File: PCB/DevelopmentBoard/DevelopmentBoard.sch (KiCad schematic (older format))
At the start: 11 parts

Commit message: Schematic Capture for RF module
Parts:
- added R? (x2): 4.7k, symbol Device:R_Small_US
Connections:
- net labels added: TBS_Crossfire_SCL, TBS_Crossfire_SDA
- wire segments 12 -> 19
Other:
- moved on the sheet: R?
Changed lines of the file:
@@
 L Device:R_Small_US R?
 U 1 1 6166A727
-P 6150 6050
-F 0 "R?" H 6218 6096 50  0000 L CNN
-F 1 "4.7k" H 6218 6005 50  0000 L CNN
-F 2 "" H 6150 6050 50  0001 C CNN
-F 3 "~" H 6150 6050 50  0001 C CNN
-	1    6150 6050
+P 6250 6050
+F 0 "R?" H 6318 6096 50  0000 L CNN
+F 1 "4.7k" H 6318 6005 50  0000 L CNN
+F 2 "" H 6250 6050 50  0001 C CNN
+F 3 "~" H 6250 6050 50  0001 C CNN
+	1    6250 6050
 	1    0    0    -1
 $EndComp
@@
 L Device:R_Small_US R?
 U 1 1 6166AB22
-P 6450 6050
-F 0 "R?" H 6518 6096 50  0000 L CNN
-F 1 "4.7k" H 6518 6005 50  0000 L CNN
-F 2 "" H 6450 6050 50  0001 C CNN
-F 3 "~" H 6450 6050 50  0001 C CNN
-	1    6450 6050
+P 6550 6050
+F 0 "R?" H 6618 6096 50  0000 L CNN
+F 1 "4.7k" H 6618 6005 50  0000 L CNN
+F 2 "" H 6550 6050 50  0001 C CNN
+F 3 "~" H 6550 6050 50  0001 C CNN
+	1    6550 6050
 	1    0    0    -1
 $EndComp
@@
 	5850 6150 5850 6750
 Wire Wire Line
-	6450 6150 6450 6750
-Text Label 6450 6150 3    50   ~ 0
+	6550 6150 6550 6750
+Text Label 6550 6150 3    50   ~ 0
 VN-100_MOSI
 Wire Wire Line
-	6150 6750 6150 6150
-Text Label 6150 6150 3    50   ~ 0
+	6250 6750 6250 6150
+Text Label 6250 6150 3    50   ~ 0
 VN-100_MISO
 $Comp
@@
 L power:+3.3V #PWR?
 U 1 1 61671A73
-P 6150 5950
-F 0 "#PWR?" H 6150 5800 50  0001 C CNN
-F 1 "+3.3V" H 6165 6123 50  0000 C CNN
-F 2 "" H 6150 5950 50  0001 C CNN
-F 3 "" H 6150 5950 50  0001 C CNN
-	1    6150 5950
+P 6250 5950
+F 0 "#PWR?" H 6250 5800 50  0001 C CNN
+F 1 "+3.3V" H 6265 6123 50  0000 C CNN
+F 2 "" H 6250 5950 50  0001 C CNN
+F 3 "" H 6250 5950 50  0001 C CNN
+	1    6250 5950
 	1    0    0    -1
 $EndComp
@@
 L power:+3.3V #PWR?
 U 1 1 61672A6F
-P 6450 5950
-F 0 "#PWR?" H 6450 5800 50  0001 C CNN
-F 1 "+3.3V" H 6465 6123 50  0000 C CNN
-F 2 "" H 6450 5950 50  0001 C CNN
-F 3 "" H 6450 5950 50  0001 C CNN
-	1    6450 5950
+P 6550 5950
+F 0 "#PWR?" H 6550 5800 50  0001 C CNN
+F 1 "+3.3V" H 6565 6123 50  0000 C CNN
+F 2 "" H 6550 5950 50  0001 C CNN
+F 3 "" H 6550 5950 50  0001 C CNN
+	1    6550 5950
 	1    0    0    -1
 $EndComp
+Wire Wire Line
+	17700 7600 17500 7600
+Connection ~ 17500 7600
+Text Label 16850 7700 0    50   ~ 0
+TBS_Crossfire_SCL
+Text Label 16850 7600 0    50   ~ 0
+TBS_Crossfire_SDA
+Wire Wire Line
+	16850 7600 17500 7600
+Wire Wire Line
+	16850 7700 17500 7700
+Text Label 10550 8150 0    50   ~ 0
+TBS_Crossfire_SCL
+Text Label 10550 8250 0    50   ~ 0
+TBS_Crossfire_SDA
+Wire Wire Line
+	10550 8250 11250 8250
+Wire Wire Line
+	10550 8150 11250 8150
+$Comp
+L Device:R_Small_US R?
+U 1 1 6160D96F
+P 5850 7300
+F 0 "R?" H 5918 7346 50  0000 L CNN
+F 1 "4.7k" H 5918 7255 50  0000 L CNN
+F 2 "" H 5850 7300 50  0001 C CNN
+F 3 "~" H 5850 7300 50  0001 C CNN
+	1    5850 7300
+	1    0    0    -1
+$EndComp
+$Comp
+L Device:R_Small_US R?
+U 1 1 6160D975
+P 6150 7300
+F 0 "R?" H 6218 7346 50  0000 L CNN
+F 1 "4.7k" H 6218 7255 50  0000 L CNN
+F 2 "" H 6150 7300 50  0001 C CNN
+F 3 "~" H 6150 7300 50  0001 C CNN
+	1    6150 7300
+	1    0    0    -1
+$EndComp
+Text Label 6150 7400 3    50   ~ 0
+TBS_Crossfire_SCL
+Text Label 5850 7400 3    50   ~ 0
+TBS_Crossfire_SDA
+$Comp
+L power:+3.3V #PWR?
+U 1 1 6160D97F
+P 5850 7200
+F 0 "#PWR?" H 5850 7050 50  0001 C CNN
+F 1 "+3.3V" H 5865 7373 50  0000 C CNN
+F 2 "" H 5850 7200 50  0001 C CNN
+F 3 "" H 5850 7200 50  0001 C CNN
+	1    5850 7200
+	1    0    0    -1
+$EndComp
+$Comp
+L power:+3.3V #PWR?
+U 1 1 6160D985
+P 6150 7200
+F 0 "#PWR?" H 6150 7050 50  0001 C CNN
+F 1 "+3.3V" H 6165 7373 50  0000 C CNN
+F 2 "" H 6150 7200 50  0001 C CNN
+F 3 "" H 6150 7200 50  0001 C CNN
+	1    6150 7200
+	1    0    0    -1
+$EndComp
+Wire Wire Line
+	6150 7400 6150 8100
+Wire Wire Line
+	5850 7400 5850 8100
+$Comp
+L power:GND #PWR?
+U 1 1 61619131
+P 18300 7400
+F 0 "#PWR?" H 18300 7150 50  0001 C CNN
+F 1 "GND" V 18305 7272 50  0000 R CNN
+F 2 "" H 18300 7400 50  0001 C CNN
+F 3 "" H 18300 7400 50  0001 C CNN
+	1    18300 7400
+	0    -1   -1   0
+$EndComp
+$Comp
+L power:GND #PWR?
+U 1 1 6161AEF3
+P 17500 7500
+F 0 "#PWR?" H 17500 7250 50  0001 C CNN
+F 1 "GND" V 17505 7372 50  0000 R CNN
+F 2 "" H 17500 7500 50  0001 C CNN
+F 3 "" H 17500 7500 50  0001 C CNN
+	1    17500 7500
+	0    1    1    0
+$EndComp
+$Comp
+L power:+5V #PWR?
+U 1 1 6161BA5A
+P 18300 7500
+F 0 "#PWR?" H 18300 7350 50  0001 C CNN
+F 1 "+5V" V 18315 7628 50  0000 L CNN
+F 2 "" H 18300 7500 50  0001 C CNN
+F 3 "" H 18300 7500 50  0001 C CNN
+	1    18300 7500
+	0    1    1    0
+$EndComp
 $EndSCHEMATC

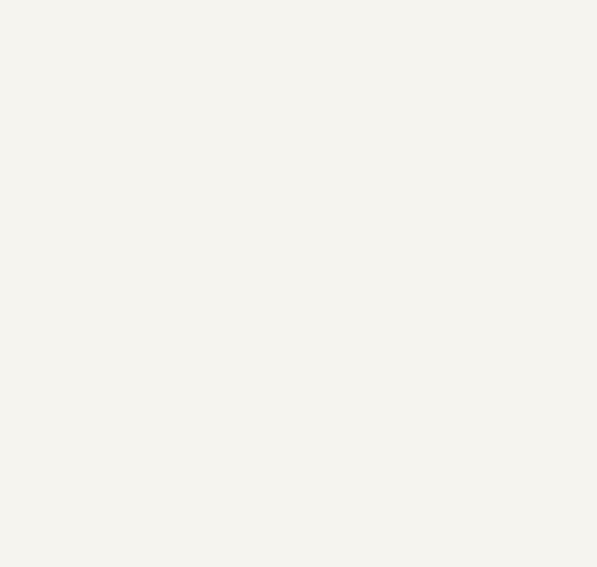
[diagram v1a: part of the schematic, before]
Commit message: Placed Micro-USB symbol on schematic
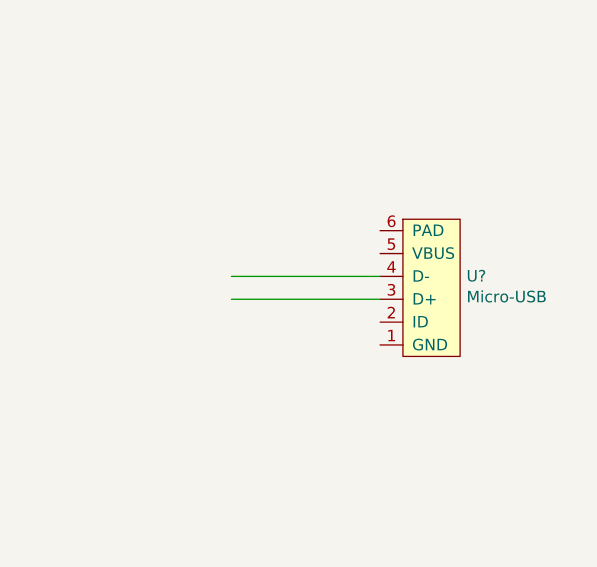
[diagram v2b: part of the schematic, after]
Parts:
- added U?: Micro-USB, symbol PayloadSymbols:Micro-USB
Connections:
- wire segments 19 -> 21
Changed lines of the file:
@@
 	0    1    1    0
 $EndComp
+$Comp
+L PayloadSymbols:Micro-USB U?
+U 1 1 615E85F0
+P 20550 7750
+F 0 "U?" H 20728 7801 50  0000 L CNN
+F 1 "Micro-USB" H 20728 7710 50  0000 L CNN
+F 2 "" H 20450 7800 50  0001 C CNN
+F 3 "" H 20450 7800 50  0001 C CNN
+	1    20550 7750
+	1    0    0    -1
+$EndComp
+Wire Wire Line
+	19700 7700 20350 7700
+Wire Wire Line
+	19700 7800 20350 7800
 $EndSCHEMATC

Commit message: USB Pins
Found and connected the USB pins on pins 103 & 105
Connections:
- net labels added: USB_D+, USB_D-
- wire segments 21 -> 23
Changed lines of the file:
@@
 Wire Wire Line
 	19700 7800 20350 7800
+Wire Wire Line
+	13400 4350 13050 4350
+Wire Wire Line
+	13400 4450 13050 4450
+Text Label 13400 4350 2    50   ~ 0
+USB_D-
+Text Label 13400 4450 2    50   ~ 0
+USB_D+
+Text Label 20200 7700 2    50   ~ 0
+USB_D-
+Text Label 20200 7800 2    50   ~ 0
+USB_D+
 $EndSCHEMATC

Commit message: Finished VN-100 Breakout Board. Removed USB from DevBoard Schematic
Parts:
- removed U?: Micro-USB, symbol PayloadSymbols:Micro-USB
- removed X?: XT30-F_Connector, symbol PayloadSymbols:XT30-F_Connector
- added X?: XT30-F_Connector, symbol PayloadSymbols:XT30-F_Connector
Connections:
- net labels removed: USB_D+, USB_D-
- wire segments 23 -> 21
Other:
- moved on the sheet: U?, X?

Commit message: Updated Dev Board Schematic
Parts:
- removed U?: VN-100, symbol PayloadSymbols:VN-100
- added R? (x12): 0, symbol Device:R_Small_US
- added U?: Micro-USB, symbol PayloadSymbols:Micro-USB
- added U?: Barometer_Grove, symbol PayloadSymbols:Barometer_Grove
- added U?: VN-100_Breakout, symbol PayloadSymbols:VN-100_Breakout
- added X?: 2mmGrove_Connector, symbol PayloadSymbols:2mmGrove_Connector
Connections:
- net labels added: D+, D-, MCU_Reset, RX, SCL, SDA, TX, VN-100_Enable
- net labels removed: TBS_Crossfire_SCL, TBS_Crossfire_SDA
- wire segments 21 -> 35
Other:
- note added: "High during ON: Reset\n"
- note added: "Low: Disable\n"
- note added: "Low: Reset"
- moved on the sheet: R?

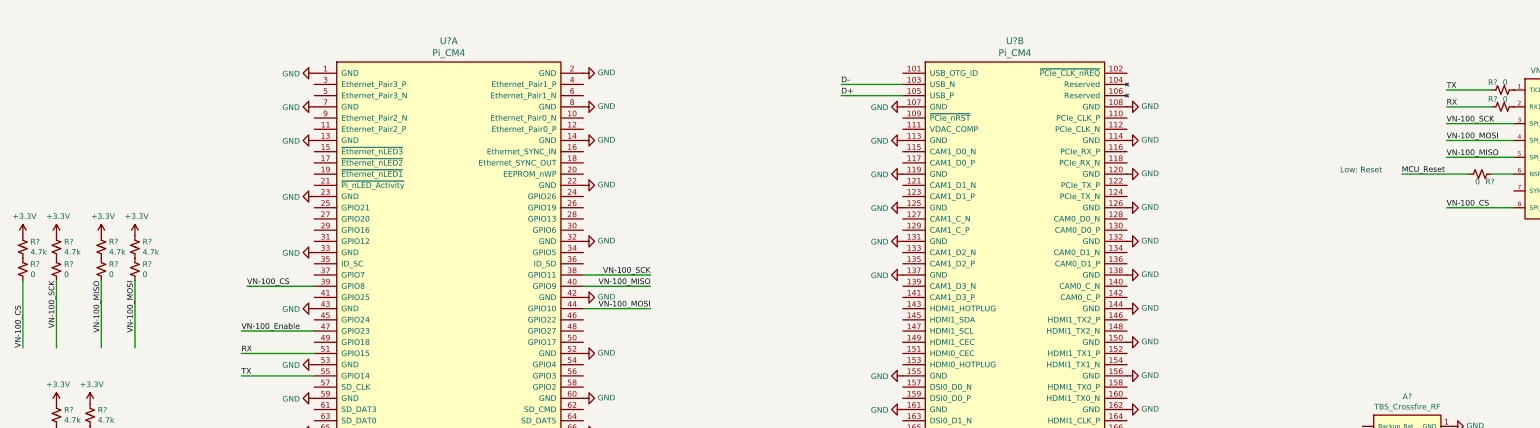
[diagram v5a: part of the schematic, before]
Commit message: Devboard changes(UART & SPI)
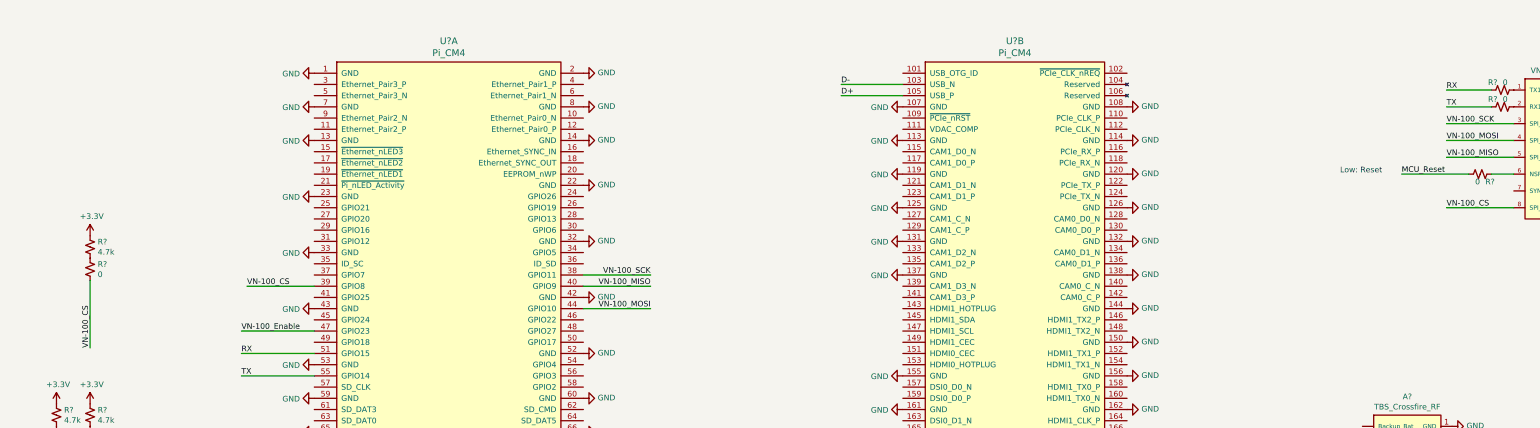
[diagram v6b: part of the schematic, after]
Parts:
- removed R? (x3): 4.7k, symbol Device:R_Small_US
- removed R? (x3): 0, symbol Device:R_Small_US
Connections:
- wire segments 35 -> 32
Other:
- moved on the sheet: R?
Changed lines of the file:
@@
-$Comp
-L Device:R_Small_US R?
-U 1 1 616692E6
-P 5850 5800
-F 0 "R?" H 5918 5846 50  0000 L CNN
-F 1 "4.7k" H 5918 5755 50  0000 L CNN
-F 2 "" H 5850 5800 50  0001 C CNN
-F 3 "~" H 5850 5800 50  0001 C CNN
-	1    5850 5800
-	1    0    0    -1
-$EndComp
-$Comp
-L Device:R_Small_US R?
-U 1 1 6166A727
-P 6250 5800
-F 0 "R?" H 6318 5846 50  0000 L CNN
-F 1 "4.7k" H 6318 5755 50  0000 L CNN
-F 2 "" H 6250 5800 50  0001 C CNN
-F 3 "~" H 6250 5800 50  0001 C CNN
-	1    6250 5800
-	1    0    0    -1
-$EndComp
-$Comp
-L Device:R_Small_US R?
-U 1 1 6166AB22
-P 6550 5800
-F 0 "R?" H 6618 5846 50  0000 L CNN
-F 1 "4.7k" H 6618 5755 50  0000 L CNN
-F 2 "" H 6550 5800 50  0001 C CNN
-F 3 "~" H 6550 5800 50  0001 C CNN
-	1    6550 5800
-	1    0    0    -1
-$EndComp
 $Comp
 L Device:R_Small_US R?
 U 1 1 6166E291
-P 5550 5800
-F 0 "R?" H 5618 5846 50  0000 L CNN
-F 1 "4.7k" H 5618 5755 50  0000 L CNN
-F 2 "" H 5550 5800 50  0001 C CNN
-F 3 "~" H 5550 5800 50  0001 C CNN
-	1    5550 5800
-	1    0    0    -1
-$EndComp
-Wire Wire Line
-	5550 6100 5550 6700
-Text Label 5550 6700 1    50   ~ 0
+P 6150 5800
+F 0 "R?" H 6218 5846 50  0000 L CNN
+F 1 "4.7k" H 6218 5755 50  0000 L CNN
+F 2 "" H 6150 5800 50  0001 C CNN
+F 3 "~" H 6150 5800 50  0001 C CNN
+	1    6150 5800
+	1    0    0    -1
+$EndComp
+Wire Wire Line
+	6150 6100 6150 6700
+Text Label 6150 6700 1    50   ~ 0
 VN-100_CS
-Text Label 5850 6100 3    50   ~ 0
-VN-100_SCK
-Wire Wire Line
-	5850 6100 5850 6700
-Wire Wire Line
-	6550 6100 6550 6700
-Text Label 6550 6100 3    50   ~ 0
-VN-100_MOSI
-Wire Wire Line
-	6250 6700 6250 6100
-Text Label 6250 6100 3    50   ~ 0
-VN-100_MISO
 $Comp
 L power:+3.3V #PWR?
 U 1 1 61670634
-P 5550 5700
-F 0 "#PWR?" H 5550 5550 50  0001 C CNN
-F 1 "+3.3V" H 5565 5873 50  0000 C CNN
-F 2 "" H 5550 5700 50  0001 C CNN
-F 3 "" H 5550 5700 50  0001 C CNN
-	1    5550 5700
-	1    0    0    -1
-$EndComp
-$Comp
-L power:+3.3V #PWR?
-U 1 1 616717DF
-P 5850 5700
-F 0 "#PWR?" H 5850 5550 50  0001 C CNN
-F 1 "+3.3V" H 5865 5873 50  0000 C CNN
-F 2 "" H 5850 5700 50  0001 C CNN
-F 3 "" H 5850 5700 50  0001 C CNN
-	1    5850 5700
-	1    0    0    -1
-$EndComp
-$Comp
-L power:+3.3V #PWR?
-U 1 1 61671A73
-P 6250 5700
-F 0 "#PWR?" H 6250 5550 50  0001 C CNN
-F 1 "+3.3V" H 6265 5873 50  0000 C CNN
-F 2 "" H 6250 5700 50  0001 C CNN
-F 3 "" H 6250 5700 50  0001 C CNN
-	1    6250 5700
-	1    0    0    -1
-$EndComp
-$Comp
-L power:+3.3V #PWR?
-U 1 1 61672A6F
-P 6550 5700
-F 0 "#PWR?" H 6550 5550 50  0001 C CNN
-F 1 "+3.3V" H 6565 5873 50  0000 C CNN
-F 2 "" H 6550 5700 50  0001 C CNN
-F 3 "" H 6550 5700 50  0001 C CNN
-	1    6550 5700
+P 6150 5700
+F 0 "#PWR?" H 6150 5550 50  0001 C CNN
+F 1 "+3.3V" H 6165 5873 50  0000 C CNN
+F 2 "" H 6150 5700 50  0001 C CNN
+F 3 "" H 6150 5700 50  0001 C CNN
+	1    6150 5700
 	1    0    0    -1
 $EndComp
@@
 $Comp
 L Device:R_Small_US R?
-U 1 1 6168741A
-P 5850 6000
-F 0 "R?" H 5918 6046 50  0000 L CNN
-F 1 "0" H 5918 5955 50  0000 L CNN
-F 2 "" H 5850 6000 50  0001 C CNN
-F 3 "~" H 5850 6000 50  0001 C CNN
-	1    5850 6000
-	1    0    0    -1
-$EndComp
-$Comp
-L Device:R_Small_US R?
-U 1 1 61687420
-P 6250 6000
-F 0 "R?" H 6318 6046 50  0000 L CNN
-F 1 "0" H 6318 5955 50  0000 L CNN
-F 2 "" H 6250 6000 50  0001 C CNN
-F 3 "~" H 6250 6000 50  0001 C CNN
-	1    6250 6000
-	1    0    0    -1
-$EndComp
-$Comp
-L Device:R_Small_US R?
-U 1 1 61687426
-P 6550 6000
-F 0 "R?" H 6618 6046 50  0000 L CNN
-F 1 "0" H 6618 5955 50  0000 L CNN
-F 2 "" H 6550 6000 50  0001 C CNN
-F 3 "~" H 6550 6000 50  0001 C CNN
-	1    6550 6000
-	1    0    0    -1
-$EndComp
-$Comp
-L Device:R_Small_US R?
 U 1 1 6168742C
-P 5550 6000
-F 0 "R?" H 5618 6046 50  0000 L CNN
-F 1 "0" H 5618 5955 50  0000 L CNN
-F 2 "" H 5550 6000 50  0001 C CNN
-F 3 "~" H 5550 6000 50  0001 C CNN
-	1    5550 6000
+P 6150 6000
+F 0 "R?" H 6218 6046 50  0000 L CNN
+F 1 "0" H 6218 5955 50  0000 L CNN
+F 2 "" H 6150 6000 50  0001 C CNN
+F 3 "~" H 6150 6000 50  0001 C CNN
+	1    6150 6000
 	1    0    0    -1
 $EndComp
@@
 RX
 Text Label 18250 4400 0    50   ~ 0
+RX
+Text Label 18250 4550 0    50   ~ 0
 TX
-Text Label 18250 4550 0    50   ~ 0
-RX
-$Comp
-L Device:R_Small_US R?
+$Comp
+L Device:R_Small_US R?
